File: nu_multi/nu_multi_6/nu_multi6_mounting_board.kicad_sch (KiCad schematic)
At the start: 7 parts, among them J13 CONN_01X14, U1 nu_capsule, U2 nu_capsule, U3 nu_capsule, U4 nu_capsule, U5 nu_capsule, U6 nu_capsule

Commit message: Use 1x7p connector from cycfi lib
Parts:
- J13: footprint Pin_Headers:Pin_Header_Straight_2x07_Pitch1.00mm_SMD -> cycfi_library:pin_header_2x7p_1.00mm_smd_vertical
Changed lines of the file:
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@@
       (effects (font (size 1.27 1.27)) hide)
     )
-    (property "Footprint" "Pin_Headers:Pin_Header_Straight_2x07_Pitch1.00mm_SMD" (id 2) (at 190.5 64.77 0)
+    (property "Footprint" "cycfi_library:pin_header_2x7p_1.00mm_smd_vertical" (id 2) (at 190.5 64.77 0)
       (effects (font (size 1.27 1.27)) hide)
     )
@@
     )
     (path "/00000000-0000-0000-0000-00005aa25edc"
-      (reference "J13") (unit 1) (value "CONN_01X14") (footprint "Pin_Headers:Pin_Header_Straight_2x07_Pitch1.00mm_SMD")
+      (reference "J13") (unit 1) (value "CONN_01X14") (footprint "cycfi_library:pin_header_2x7p_1.00mm_smd_vertical")
     )
     (path "/09c5aab3-f4a7-4ad0-af7b-ac955e31a570"

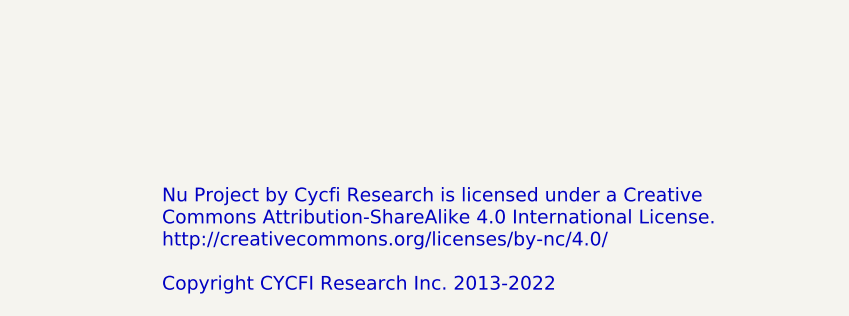
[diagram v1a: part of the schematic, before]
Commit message: - Upgrade to Kicad 8 - Update board to v2.53, minor edits,
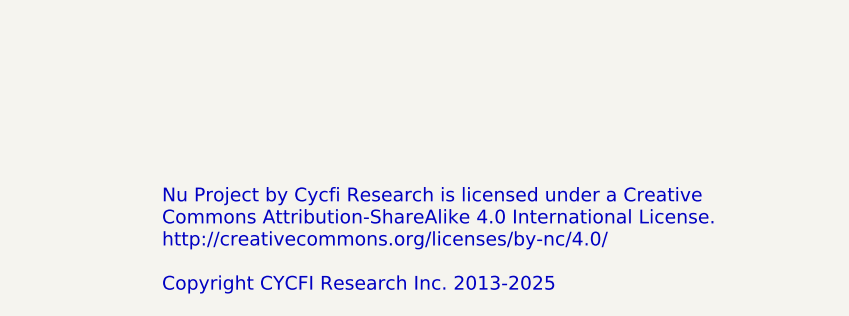
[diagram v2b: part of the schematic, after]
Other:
- note added: "Nu Project by Cycfi Research is licensed under a Creative Commons Attribution-ShareAlike 4.0 International License. http://creativecommons.org/licenses/by-nc/4.0/ Copyright CYCFI Research Inc. 2013-2025"
- note removed: "Nu Project by Cycfi Research is licensed under a Creative Commons Attribution-ShareAlike 4.0 International License. http://creativecommons.org/licenses/by-nc/4.0/ Copyright CYCFI Research Inc. 2013-2022"
